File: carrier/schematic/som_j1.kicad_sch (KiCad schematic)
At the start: 1 part, among them J17001 DF40C-100DS-0.4V(51)

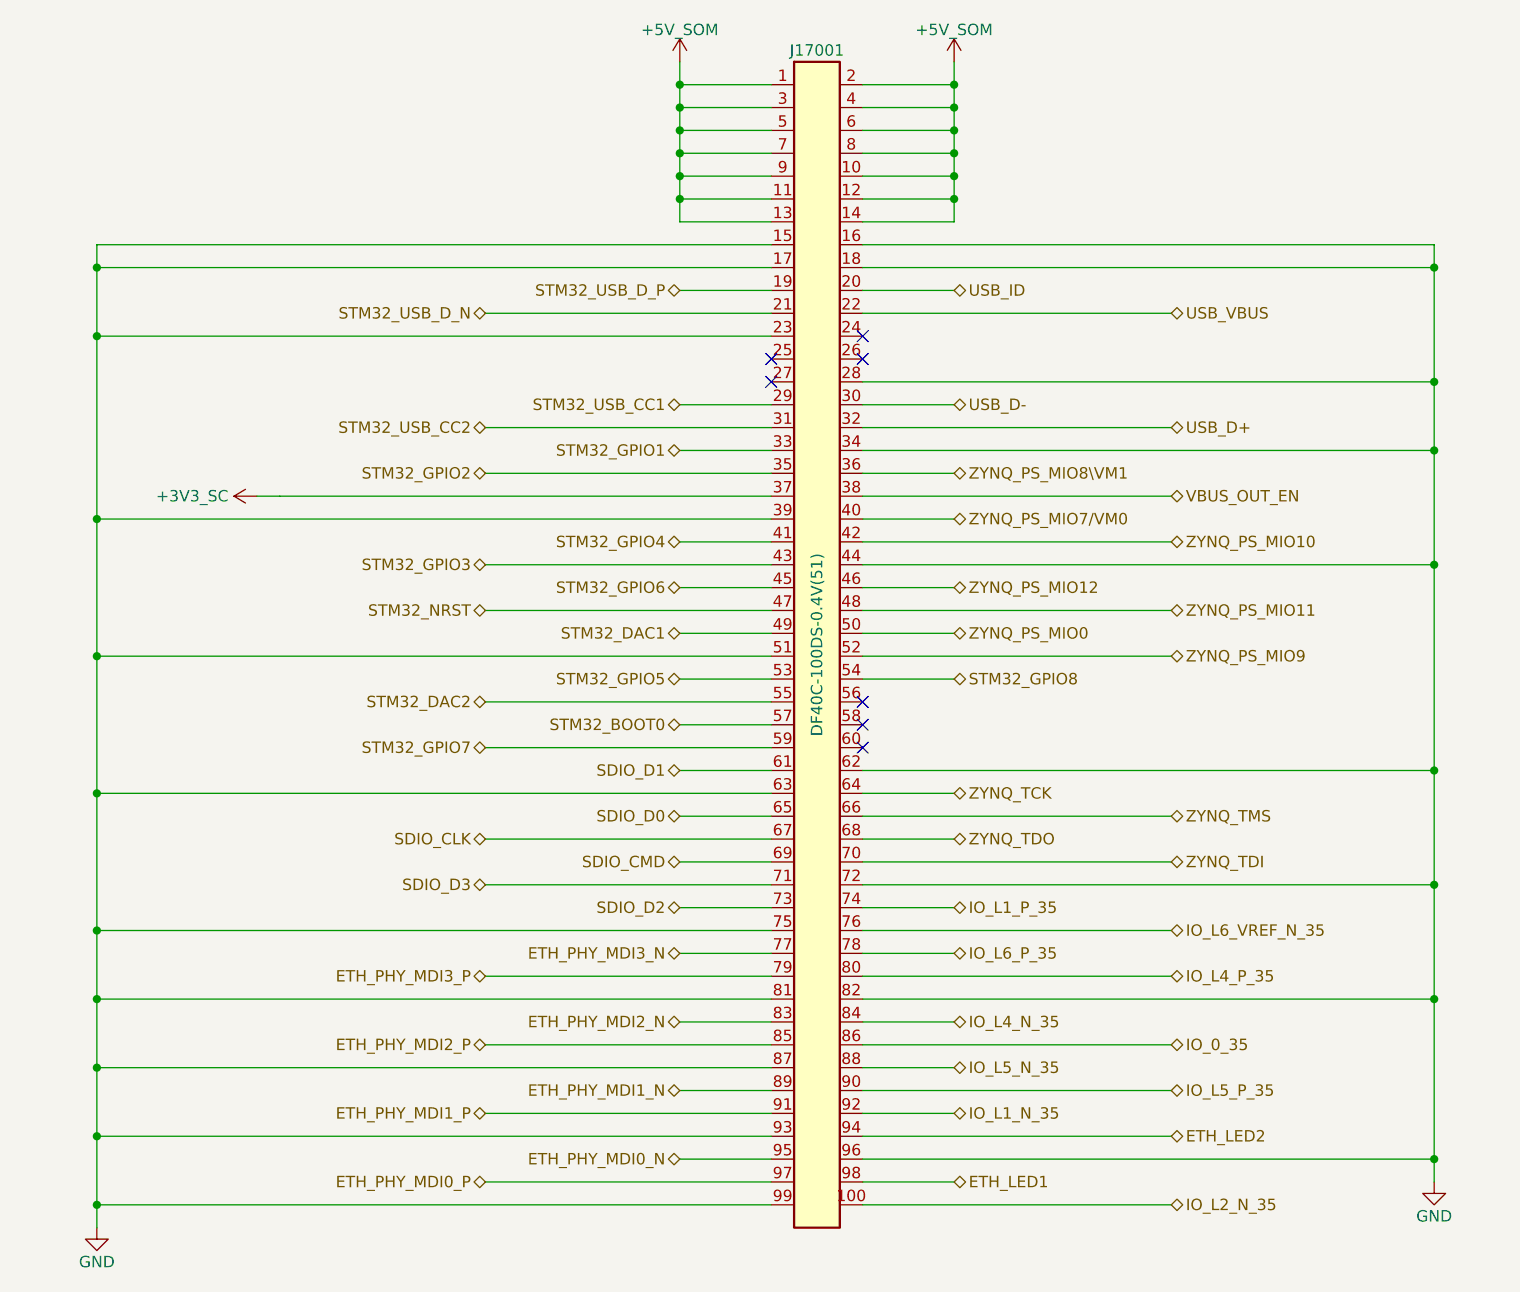
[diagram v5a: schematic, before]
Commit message: wave3(function-map): harvest — retire 109/121 cross-sheet deferrals
som_conn_gen FUNCTION_MAP emits carrier function names on J1/J2/J3 (RAIL_EN
GPIOs, SC_INT_N wire-OR [usb_pd R1 dropped, single +3V3_SC pull-up], bit-bang
I2C2 on DAC1/2, USBOTG_FLT_N->TCA9535 P14 with +3V3_SC re-rail abs-max fix,
PMON_ALERT->P11, SD_CD/LCD_CTP/HDMI/camera/FMC/PL_BTN binds, PUDC_34 strap,
VADJ 0.40->0.35A). xdc/firmware/link follow the same map. LINK 0 unbound,
12 intentionally-future deferrals (wave-2 RJ45/USB + EN_LCD_BL). Validated by
the HARDENED gates from the engine-fix harvest; goldens som_j2+bringup_rails
re-blessed after eyeball (clean); board byte-deterministic, selftest 44/44.

Co-Authored-By: Claude Fable 5 <noreply@anthropic.com>
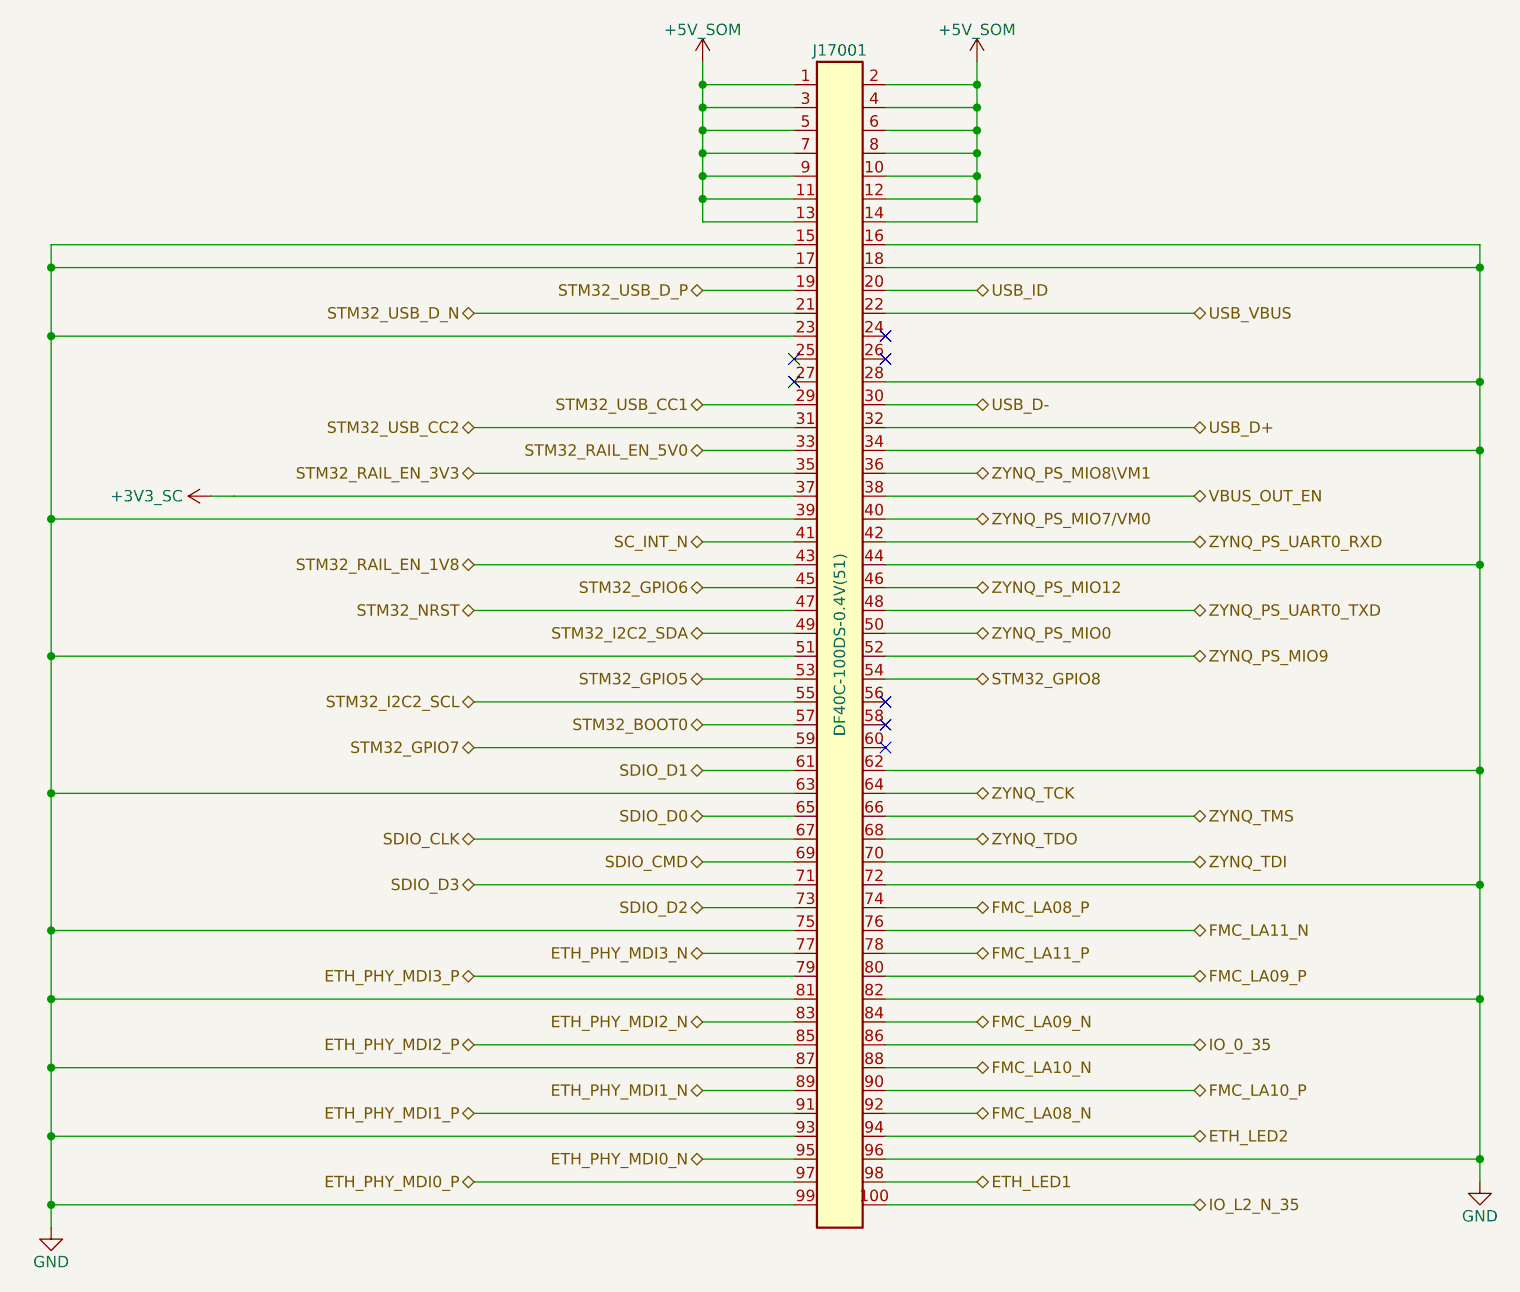
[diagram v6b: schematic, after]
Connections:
- net IO_L1_N_35 renamed FMC_LA08_N
- net IO_L1_P_35 renamed FMC_LA08_P
- net IO_L4_N_35 renamed FMC_LA09_N
- net IO_L4_P_35 renamed FMC_LA09_P
- net IO_L5_N_35 renamed FMC_LA10_N
- net IO_L5_P_35 renamed FMC_LA10_P
- net IO_L6_P_35 renamed FMC_LA11_P
- net IO_L6_VREF_N_35 renamed FMC_LA11_N
- net STM32_DAC1 renamed STM32_I2C2_SDA
- net STM32_DAC2 renamed STM32_I2C2_SCL
- net STM32_GPIO1 renamed STM32_RAIL_EN_5V0
- net STM32_GPIO2 renamed STM32_RAIL_EN_3V3
- net STM32_GPIO3 renamed STM32_RAIL_EN_1V8
- net STM32_GPIO4 renamed SC_INT_N
- net ZYNQ_PS_MIO10 renamed ZYNQ_PS_UART0_RXD
- net ZYNQ_PS_MIO11 renamed ZYNQ_PS_UART0_TXD
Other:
- moved on the sheet: J17001

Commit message: carrier: harvest wave-2 connectors — rj45_connector + usb_uart_connector (ETH-1, USBUART-1)
Plain 8P8C RJ45 (KH-5224-8P8C-D, magnetics are discrete on-board) binds the 8
ETH_LINE_MDI_* line-side ports (T568 1-2/3-6/4-5/7-8); USB-C UFP console port
(5.1k Rd device-role, USBLC6 ESD, 10u Cbus) binds USB_UART_VBUS/DP/DM. Deferrals
12->1 (only EN_LCD_BL remains), 0 unbound SoM nets. 25 sheets, LINK 0/0, BOARD
GATE PASS, selftest 44/44, both new renders eyeballed clean, goldens blessed.

Co-Authored-By: Claude Fable 5 <noreply@anthropic.com>
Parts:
- renumbered J17001 to J18001
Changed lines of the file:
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@@
 		(property
 			"Reference"
-			"J17001"
+			"J18001"
 			(at 157.48 26.67 0)
 			(effects
@@
 				(path
 					"/c2797150-7a6e-556a-82f5-fdda13c31368/cb8332a7-7e9d-541e-92f8-4b378fa3e437"
-					(reference "J17001")
+					(reference "J18001")
 					(unit 1)
 				)
@@
 		(property
 			"Reference"
-			"#PWR17001"
+			"#PWR18001"
 			(at 142.24 25.4 0)
 			(effects
@@
 				(path
 					"/c2797150-7a6e-556a-82f5-fdda13c31368/cb8332a7-7e9d-541e-92f8-4b378fa3e437"
-					(reference "#PWR17001")
+					(reference "#PWR18001")
 					(unit 1)
 				)
@@
 		(property
 			"Reference"
-			"#PWR17002"
+			"#PWR18002"
 			(at 87.63 73.66 0)
 			(effects
@@
 				(path
 					"/c2797150-7a6e-556a-82f5-fdda13c31368/cb8332a7-7e9d-541e-92f8-4b378fa3e437"
-					(reference "#PWR17002")
+					(reference "#PWR18002")
 					(unit 1)
 				)
@@
 		(property
 			"Reference"
-			"#PWR17003"
+			"#PWR18003"
 			(at 69.85 154.94 0)
 			(effects
@@
 				(path
 					"/c2797150-7a6e-556a-82f5-fdda13c31368/cb8332a7-7e9d-541e-92f8-4b378fa3e437"
-					(reference "#PWR17003")
+					(reference "#PWR18003")
 					(unit 1)
 				)
@@
 		(property
 			"Reference"
-			"#PWR17004"
+			"#PWR18004"
 			(at 172.72 25.4 0)
 			(effects
@@
 				(path
 					"/c2797150-7a6e-556a-82f5-fdda13c31368/cb8332a7-7e9d-541e-92f8-4b378fa3e437"
-					(reference "#PWR17004")
+					(reference "#PWR18004")
 					(unit 1)
 				)
@@
 		(property
 			"Reference"
-			"#PWR17005"
+			"#PWR18005"
 			(at 228.6 149.86 0)
 			(effects
@@
 				(path
 					"/c2797150-7a6e-556a-82f5-fdda13c31368/cb8332a7-7e9d-541e-92f8-4b378fa3e437"
-					(reference "#PWR17005")
+					(reference "#PWR18005")
 					(unit 1)
 				)

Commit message: DEF-6: netlist the HDMI-RX TMDS sink termination (new hdmi_rx_term sheet)
The HDMI-RX sink REQUIRES 8x 49.9 ohm/pair-to-AVCC source termination (a
7-series HR bank does not self-terminate TMDS_33) — without it HDMI RX simply
does not work. It had been carried for rounds as a docstring-only MANDATORY
layout note because the resistors belong at the FPGA-bank (receiver) end and
the connector-sheet placer could not anchor an off-sheet AVCC trunk. DEF-6
promotes it to a real, netlisted, gate-checked, BOM-counted network on its own
sheet hdmi_rx_term.py: 8x 49.9R (C114625) from HDMI_RX_{D2,D1,D0,CLK}_{P,N} to
AVCC = +3V3 (bank-33 VCCO IS +3V3, the correct TMDS_33 termination voltage).

LINK PASS (the 3-way TMDS merge with hdmi_rx + som_j2), powertree accepts the
~64 mA termination load, render clean (LAW 1), board PASS 26 sheets,
deterministic, selftest 44/44, m1 PASS.

The 100n/1u AVCC bypass is a documented layout note (not netlisted): the
placer has no pattern for a rail-to-rail cap with no host part on an IC-less
sheet (a tracked placer-robustness follow-up). Inserting the sheet
alphabetically re-stamps the per-sheet reference uniquification of the 15
downstream sheets (U11001->U12001 etc.) — deterministic, a known consequence
of the position-based hierarchy numbering.

Co-Authored-By: Claude Opus 4.8 <noreply@anthropic.com>
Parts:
- renumbered J18001 to J19001
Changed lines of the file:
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@@
 		(property
 			"Reference"
-			"J18001"
+			"J19001"
 			(at 157.48 26.67 0)
 			(effects
@@
 				(path
 					"/c2797150-7a6e-556a-82f5-fdda13c31368/cb8332a7-7e9d-541e-92f8-4b378fa3e437"
-					(reference "J18001")
+					(reference "J19001")
 					(unit 1)
 				)
@@
 		(property
 			"Reference"
-			"#PWR18001"
+			"#PWR19001"
 			(at 142.24 25.4 0)
 			(effects
@@
 				(path
 					"/c2797150-7a6e-556a-82f5-fdda13c31368/cb8332a7-7e9d-541e-92f8-4b378fa3e437"
-					(reference "#PWR18001")
+					(reference "#PWR19001")
 					(unit 1)
 				)
@@
 		(property
 			"Reference"
-			"#PWR18002"
+			"#PWR19002"
 			(at 87.63 73.66 0)
 			(effects
@@
 				(path
 					"/c2797150-7a6e-556a-82f5-fdda13c31368/cb8332a7-7e9d-541e-92f8-4b378fa3e437"
-					(reference "#PWR18002")
+					(reference "#PWR19002")
 					(unit 1)
 				)
@@
 		(property
 			"Reference"
-			"#PWR18003"
+			"#PWR19003"
 			(at 69.85 154.94 0)
 			(effects
@@
 				(path
 					"/c2797150-7a6e-556a-82f5-fdda13c31368/cb8332a7-7e9d-541e-92f8-4b378fa3e437"
-					(reference "#PWR18003")
+					(reference "#PWR19003")
 					(unit 1)
 				)
@@
 		(property
 			"Reference"
-			"#PWR18004"
+			"#PWR19004"
 			(at 172.72 25.4 0)
 			(effects
@@
 				(path
 					"/c2797150-7a6e-556a-82f5-fdda13c31368/cb8332a7-7e9d-541e-92f8-4b378fa3e437"
-					(reference "#PWR18004")
+					(reference "#PWR19004")
 					(unit 1)
 				)
@@
 		(property
 			"Reference"
-			"#PWR18005"
+			"#PWR19005"
 			(at 228.6 149.86 0)
 			(effects
@@
 				(path
 					"/c2797150-7a6e-556a-82f5-fdda13c31368/cb8332a7-7e9d-541e-92f8-4b378fa3e437"
-					(reference "#PWR18005")
+					(reference "#PWR19005")
 					(unit 1)
 				)
